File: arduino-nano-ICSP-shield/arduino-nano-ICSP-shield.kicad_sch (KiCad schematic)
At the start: 2 parts, among them J1 Analog, J2 Digital

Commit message: init led's
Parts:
- added D1, D2, D3: LED, LED_SMD:LED_0805_2012Metric_Pad1.15x1.40mm_HandSolder, symbol Device:LED
- added R1, R2, R3: R, Resistor_SMD:R_0805_2012Metric_Pad1.20x1.40mm_HandSolder, symbol Device:R
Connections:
- net GND: now also R1.1, R2.1, R3.1
- net *D9 renamed heartbeat
- net heartbeat: now also D1.2 (A)
- net D7 renamed programming
- net programming: now also D3.2 (A)
- net D8 renamed error
- net error: now also D2.2 (A)
- new net: D2.1 (K), R2.2
- new net: D3.1 (K), R3.2
- new net: D1.1 (K), R1.2

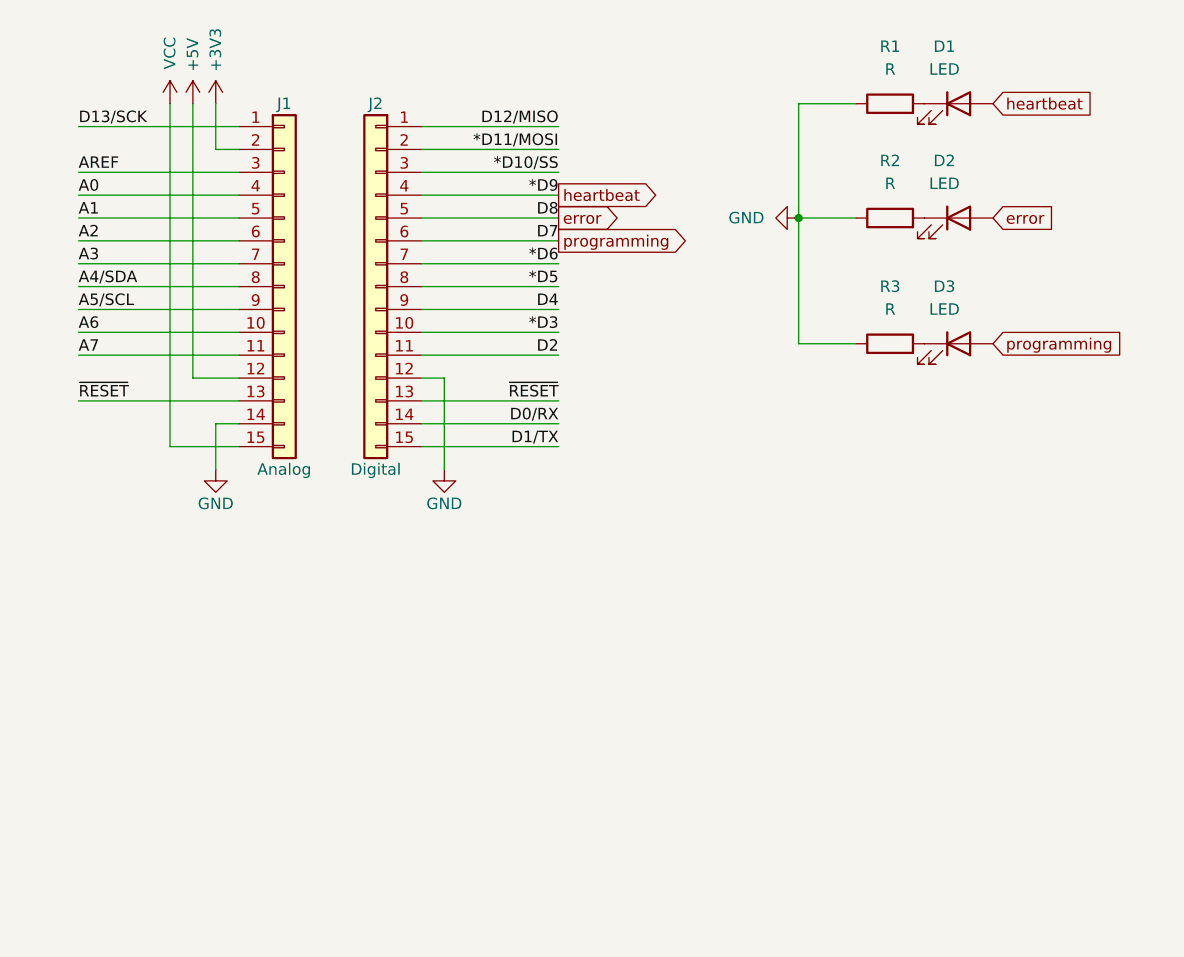
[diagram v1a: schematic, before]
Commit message: add ports
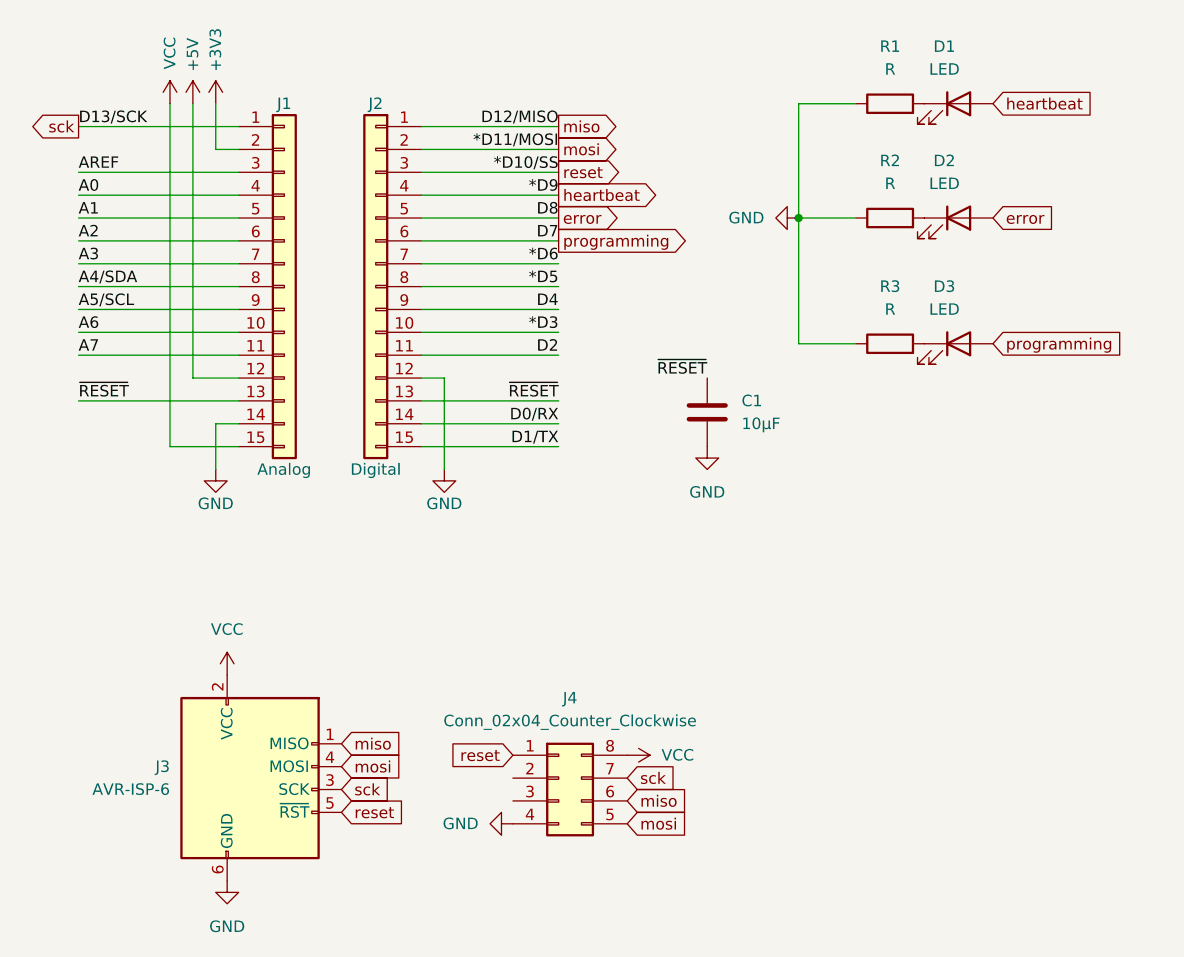
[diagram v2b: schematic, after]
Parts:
- added C1: 10µF, Capacitor_SMD:C_0805_2012Metric_Pad1.18x1.45mm_HandSolder, symbol Device:C
- added J3: AVR-ISP-6, Connector_IDC:IDC-Header_2x03_P2.54mm_Vertical, symbol Connector:AVR-ISP-6
- added J4: Conn_02x04_Counter_Clockwise, CustomLibrary:PinHeader_2x04_P2.54mm_Vertical_Counterclockwise, symbol Connector_Generic:Conn_02x04_Counter_Clockwise
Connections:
- net GND: now also C1.2, J3.6 (GND), J4.4 (Pin_4)
- net VCC: now also J3.2 (VCC), J4.8 (Pin_8)
- net ~{RESET}: now also C1.1
- net *D10/SS renamed reset
- net reset: now also J3.5 (~{RST}), J4.1 (Pin_1)
- net *D11/MOSI renamed mosi
- net mosi: now also J3.4 (MOSI), J4.5 (Pin_5)
- net D12/MISO renamed miso
- net miso: now also J3.1 (MISO), J4.6 (Pin_6)
- net D13/SCK renamed sck
- net sck: now also J3.3 (SCK), J4.7 (Pin_7)

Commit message: single header
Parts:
- J3: footprint Connector_IDC:IDC-Header_2x03_P2.54mm_Vertical -> CustomLibrary:IDC-Header_2x03_P2.54mm_Vertical-ICSP-6
- J4: footprint CustomLibrary:PinHeader_2x04_P2.54mm_Vertical_Counterclockwise -> CustomLibrary:PinHeader_2x04_P2.54mm_Vertical_Counterclockwise-Clip; now not fitted; now left out of the parts list
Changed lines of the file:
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@@
 			)
 		)
-		(property "Footprint" "Connector_IDC:IDC-Header_2x03_P2.54mm_Vertical"
+		(property "Footprint" "CustomLibrary:IDC-Header_2x03_P2.54mm_Vertical-ICSP-6"
 			(at 30.48 99.06 90)
 			(effects
@@
 		(at 71.12 99.06 0)
 		(unit 1)
-		(exclude_from_sim no)
-		(in_bom yes)
-		(on_board yes)
-		(dnp no)
+		(exclude_from_sim yes)
+		(in_bom no)
+		(on_board no)
+		(dnp yes)
 		(fields_autoplaced yes)
 		(property "Reference" "J4"
@@
 			)
 		)
-		(property "Footprint" "CustomLibrary:PinHeader_2x04_P2.54mm_Vertical_Counterclockwise"
+		(property "Footprint" "CustomLibrary:PinHeader_2x04_P2.54mm_Vertical_Counterclockwise-Clip"
 			(at 71.12 99.06 0)
 			(effects

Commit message: stuff
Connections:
- net GND: now also D1.1 (K), D2.1 (K), D3.1 (K); no longer R1.1, R2.1, R3.1
- net error: now also R2.1; no longer D2.2 (A)
- net heartbeat: now also R1.1; no longer D1.2 (A)
- net programming: now also R3.1; no longer D3.2 (A)
- net at R2.2: now also D2.2 (A); no longer D2.1 (K)
- net at R3.2: now also D3.2 (A); no longer D3.1 (K)
- net at R1.2: now also D1.2 (A); no longer D1.1 (K)
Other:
- moved on the sheet: D1, D2, D3, R1, R2, R3

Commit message: continue
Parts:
- removed R2, R3: R, Resistor_SMD:R_0805_2012Metric_Pad1.20x1.40mm_HandSolder, symbol Device:R
- C1: footprint Capacitor_SMD:C_0805_2012Metric_Pad1.18x1.45mm_HandSolder -> Capacitor_SMD:C_0603_1608Metric
- D1, D2, D3: footprint LED_SMD:LED_0805_2012Metric_Pad1.15x1.40mm_HandSolder -> LED_SMD:LED_0603_1608Metric
- R1: value R -> 140Ω; footprint Resistor_SMD:R_0805_2012Metric_Pad1.20x1.40mm_HandSolder -> Resistor_SMD:R_0603_1608Metric
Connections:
- net GND: now also R1.2; no longer D1.1 (K), D2.1 (K), D3.1 (K)
- net error: now also D2.2 (A)
- net heartbeat: now also D1.2 (A); no longer R1.1
- net programming: now also D3.2 (A)
- new net: D1.1 (K), D2.1 (K), D3.1 (K), R1.1
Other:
- moved on the sheet: D1, D2, D3, R1

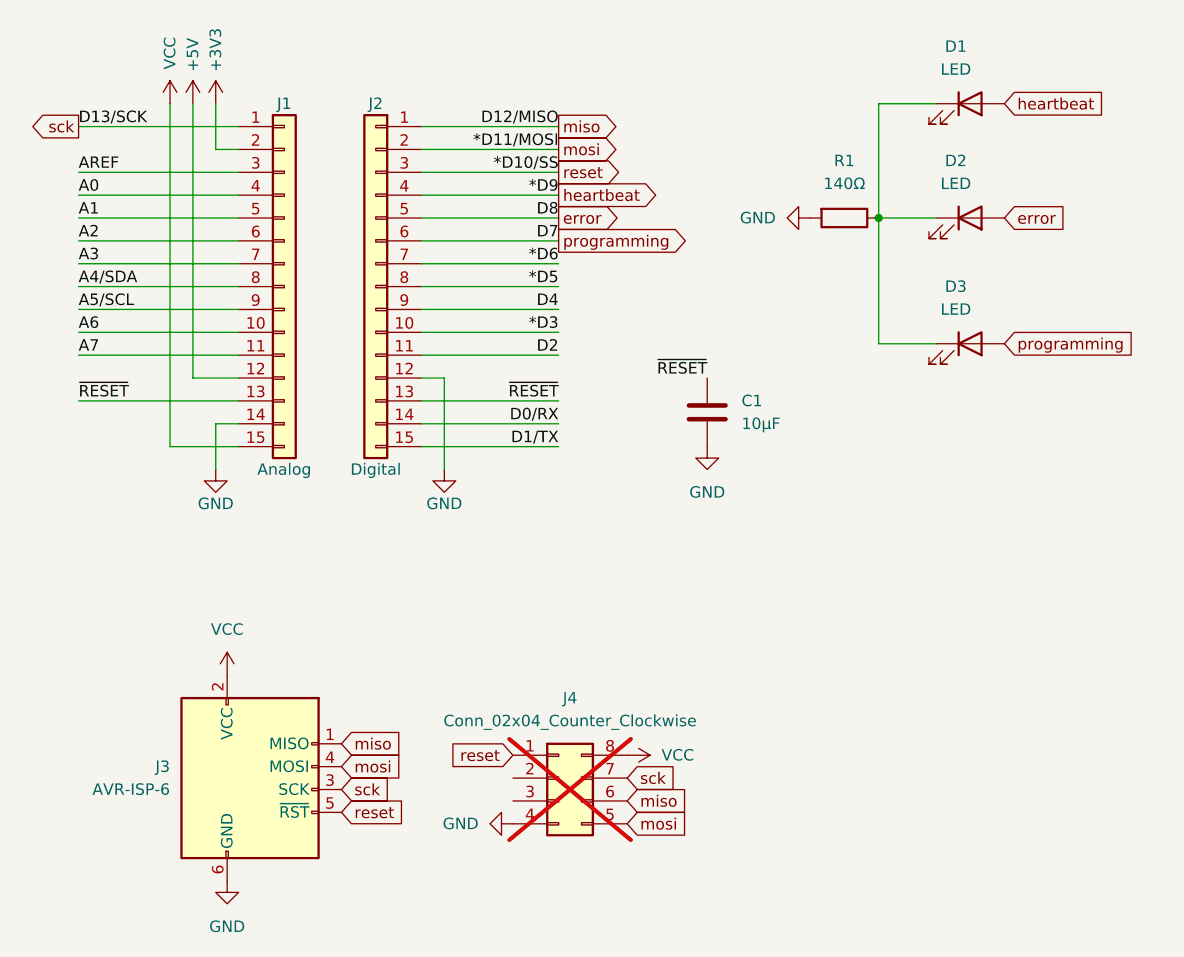
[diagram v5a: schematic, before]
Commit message: remove linked pins & route
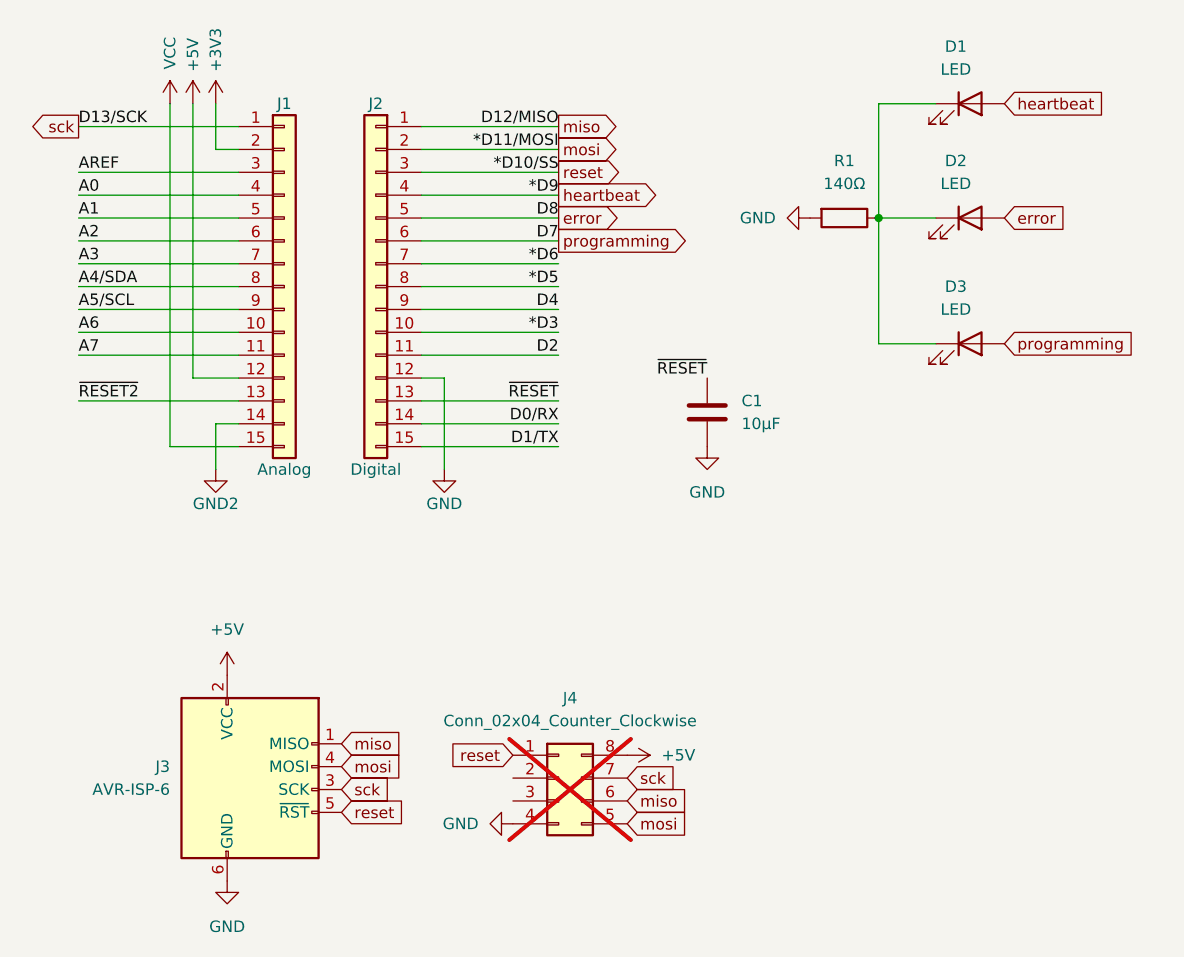
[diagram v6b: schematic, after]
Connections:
- net +5V: now also J3.2 (VCC), J4.8 (Pin_8)
- net GND: no longer J1.14 (Pin_14)
- net VCC: no longer J3.2 (VCC), J4.8 (Pin_8)
- net ~{RESET}: no longer J1.13 (Pin_13)
- new net GND2: J1.14 (Pin_14)
- new net ~{RESET2}: J1.13 (Pin_13)
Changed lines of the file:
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@@
 		)
 	)
-	(label "~{RESET}"
+	(label "~{RESET2}"
 		(at 17.78 57.15 0)
 		(effects
@@
 	)
 	(symbol
+		(lib_id "power:+5V")
+		(at 34.29 87.63 0)
+		(unit 1)
+		(exclude_from_sim no)
+		(in_bom yes)
+		(on_board yes)
+		(dnp no)
+		(fields_autoplaced yes)
+		(property "Reference" "#PWR07"
+			(at 34.29 91.44 0)
+			(effects
+				(font
+					(size 1.27 1.27)
+				)
+				(hide yes)
+			)
+		)
+		(property "Value" "+5V"
+			(at 34.29 82.55 0)
+			(effects
+				(font
+					(size 1.27 1.27)
+				)
+			)
+		)
+		(property "Footprint" ""
+			(at 34.29 87.63 0)
+			(effects
+				(font
+					(size 1.27 1.27)
+				)
+				(hide yes)
+			)
+		)
+		(property "Datasheet" ""
+			(at 34.29 87.63 0)
+			(effects
+				(font
+					(size 1.27 1.27)
+				)
+				(hide yes)
+			)
+		)
+		(property "Description" "Power symbol creates a global label with name \"+5V\""
+			(at 34.29 87.63 0)
+			(effects
+				(font
+					(size 1.27 1.27)
+				)
+				(hide yes)
+			)
+		)
+		(pin "1"
+		)
+		(instances
+			(project ""
+				(path "/0d35483a-0b12-46cc-b9f2-896fd6831779"
+					(reference "#PWR07")
+					(unit 1)
+				)
+			)
+		)
+	)
+	(symbol
 		(lib_id "power:VCC")
 		(at 27.94 24.13 0)
@@
 	)
 	(symbol
+		(lib_id "power:+5V")
+		(at 78.74 96.52 270)
+		(unit 1)
+		(exclude_from_sim no)
+		(in_bom yes)
+		(on_board yes)
+		(dnp no)
+		(fields_autoplaced yes)
+		(property "Reference" "#PWR08"
+			(at 74.93 96.52 0)
+			(effects
+				(font
+					(size 1.27 1.27)
+				)
+				(hide yes)
+			)
+		)
+		(property "Value" "+5V"
+			(at 82.55 96.5199 90)
+			(effects
+				(font
+					(size 1.27 1.27)
+				)
+				(justify left)
+			)
+		)
+		(property "Footprint" ""
+			(at 78.74 96.52 0)
+			(effects
+				(font
+					(size 1.27 1.27)
+				)
+				(hide yes)
+			)
+		)
+		(property "Datasheet" ""
+			(at 78.74 96.52 0)
+			(effects
+				(font
+					(size 1.27 1.27)
+				)
+				(hide yes)
+			)
+		)
+		(property "Description" "Power symbol creates a global label with name \"+5V\""
+			(at 78.74 96.52 0)
+			(effects
+				(font
+					(size 1.27 1.27)
+				)
+				(hide yes)
+			)
+		)
+		(pin "1"
+		)
+		(instances
+			(project "arduino-nano-ICSP-shield"
+				(path "/0d35483a-0b12-46cc-b9f2-896fd6831779"
+					(reference "#PWR08")
+					(unit 1)
+				)
+			)
+		)
+	)
+	(symbol
 		(lib_id "power:GND")
 		(at 66.04 104.14 270)
@@
 	)
 	(symbol
-		(lib_id "power:VCC")
-		(at 78.74 96.52 270)
-		(unit 1)
-		(exclude_from_sim no)
-		(in_bom yes)
-		(on_board yes)
-		(dnp no)
-		(fields_autoplaced yes)
-		(property "Reference" "#PWR05"
-			(at 74.93 96.52 0)
-			(effects
-				(font
-					(size 1.27 1.27)
-				)
-				(hide yes)
-			)
-		)
-		(property "Value" "VCC"
-			(at 82.55 96.5199 90)
-			(effects
-				(font
-					(size 1.27 1.27)
-				)
-				(justify left)
-			)
-		)
-		(property "Footprint" ""
-			(at 78.74 96.52 0)
-			(effects
-				(font
-					(size 1.27 1.27)
-				)
-				(hide yes)
-			)
-		)
-		(property "Datasheet" ""
-			(at 78.74 96.52 0)
-			(effects
-				(font
-					(size 1.27 1.27)
-				)
-				(hide yes)
-			)
-		)
-		(property "Description" "Power symbol creates a global label with name \"VCC\""
-			(at 78.74 96.52 0)
-			(effects
-				(font
-					(size 1.27 1.27)
-				)
-				(hide yes)
-			)
-		)
-		(pin "1"
-		)
-		(instances
-			(project "arduino-nano-ICSP-shield"
-				(path "/0d35483a-0b12-46cc-b9f2-896fd6831779"
-					(reference "#PWR05")
-					(unit 1)
-				)
-			)
-		)
-	)
-	(symbol
 		(lib_id "power:GND")
 		(at 33.02 64.77 0)
@@
 			)
 		)
-		(property "Value" "GND"
+		(property "Value" "GND2"
 			(at 33.02 68.58 0)
 			(effects
@@
 					(unit 1)
 				)
-			)
-		)
-	)
-	(symbol
-		(lib_id "power:VCC")
-		(at 34.29 87.63 0)
-		(unit 1)
-		(exclude_from_sim no)
-		(in_bom yes)
-		(on_board yes)
-		(dnp no)
-		(fields_autoplaced yes)
-		(property "Reference" "#PWR03"
-			(at 34.29 91.44 0)
-			(effects
-				(font
-					(size 1.27 1.27)
-				)
-				(hide yes)
-			)
-		)
-		(property "Value" "VCC"
-			(at 34.29 82.55 0)
-			(effects
-				(font
-					(size 1.27 1.27)
-				)
-			)
-		)
-		(property "Footprint" ""
-			(at 34.29 87.63 0)
-			(effects
-				(font
-					(size 1.27 1.27)
-				)
-				(hide yes)
-			)
-		)
-		(property "Datasheet" ""
-			(at 34.29 87.63 0)
-			(effects
-				(font
-					(size 1.27 1.27)
-				)
-				(hide yes)
-			)
-		)
-		(property "Description" "Power symbol creates a global label with name \"VCC\""
-			(at 34.29 87.63 0)
-			(effects
-				(font
-					(size 1.27 1.27)
-				)
-				(hide yes)
-			)
-		)
-		(pin "1"
-		)
-		(instances
-			(project ""
-				(path "/0d35483a-0b12-46cc-b9f2-896fd6831779"
-					(reference "#PWR03")
-					(unit 1)
-				)

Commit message: flip resistor
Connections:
- net GND: now also R1.1; no longer R1.2
- net at D1.1 (K), D2.1 (K), D3.1 (K): now also R1.2; no longer R1.1
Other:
- moved on the sheet: R1
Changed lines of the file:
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@@
 	(symbol
 		(lib_id "Device:R")
-		(at 102.87 36.83 270)
+		(at 102.87 36.83 90)
 		(unit 1)
 		(exclude_from_sim no)
@@
 		)
 		(property "Footprint" "Resistor_SMD:R_0603_1608Metric"
-			(at 102.87 35.052 90)
+			(at 102.87 38.608 90)
 			(effects
 				(font

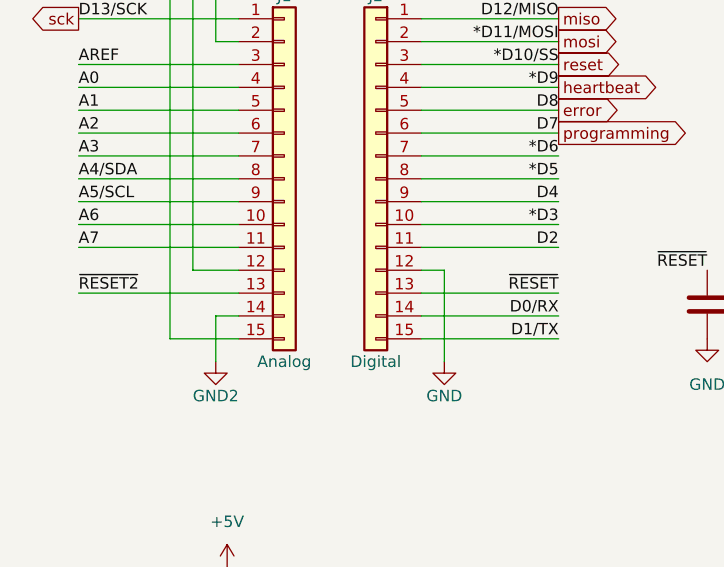
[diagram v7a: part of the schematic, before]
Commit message: routed by hand
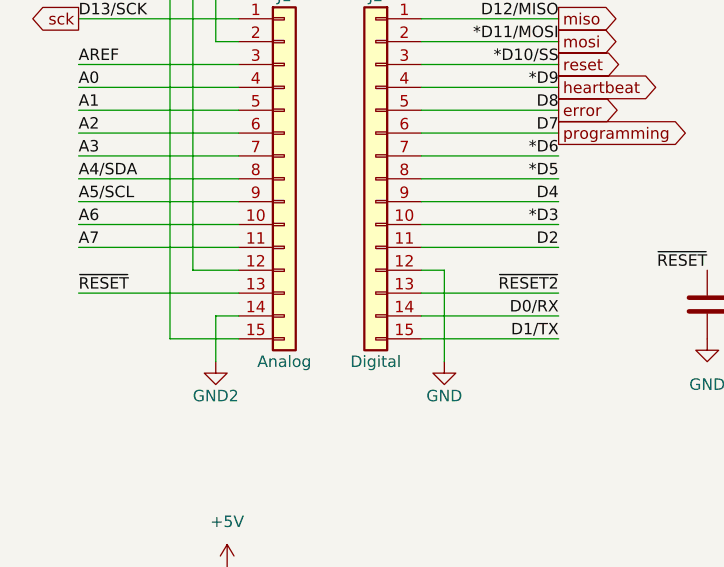
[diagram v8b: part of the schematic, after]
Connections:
- net ~{RESET2}: now also J2.13 (Pin_13); no longer J1.13 (Pin_13)
- net ~{RESET}: now also J1.13 (Pin_13); no longer J2.13 (Pin_13)
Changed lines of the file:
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@@
 		)
 	)
-	(label "~{RESET}"
+	(label "~{RESET2}"
 		(at 71.12 57.15 180)
 		(effects
@@
 		)
 	)
-	(label "~{RESET2}"
+	(label "~{RESET}"
 		(at 17.78 57.15 0)
 		(effects
